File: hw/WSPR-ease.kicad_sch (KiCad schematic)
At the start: 44 parts, among them J101 pwr+data, J102 SMA, J103 SMA, Q101 MMBF170, U101 SRV05-4, U102 ESP32-S3-WROOM-1-N8R8, U103 LMR51430YDDCR, U104 GNSS module

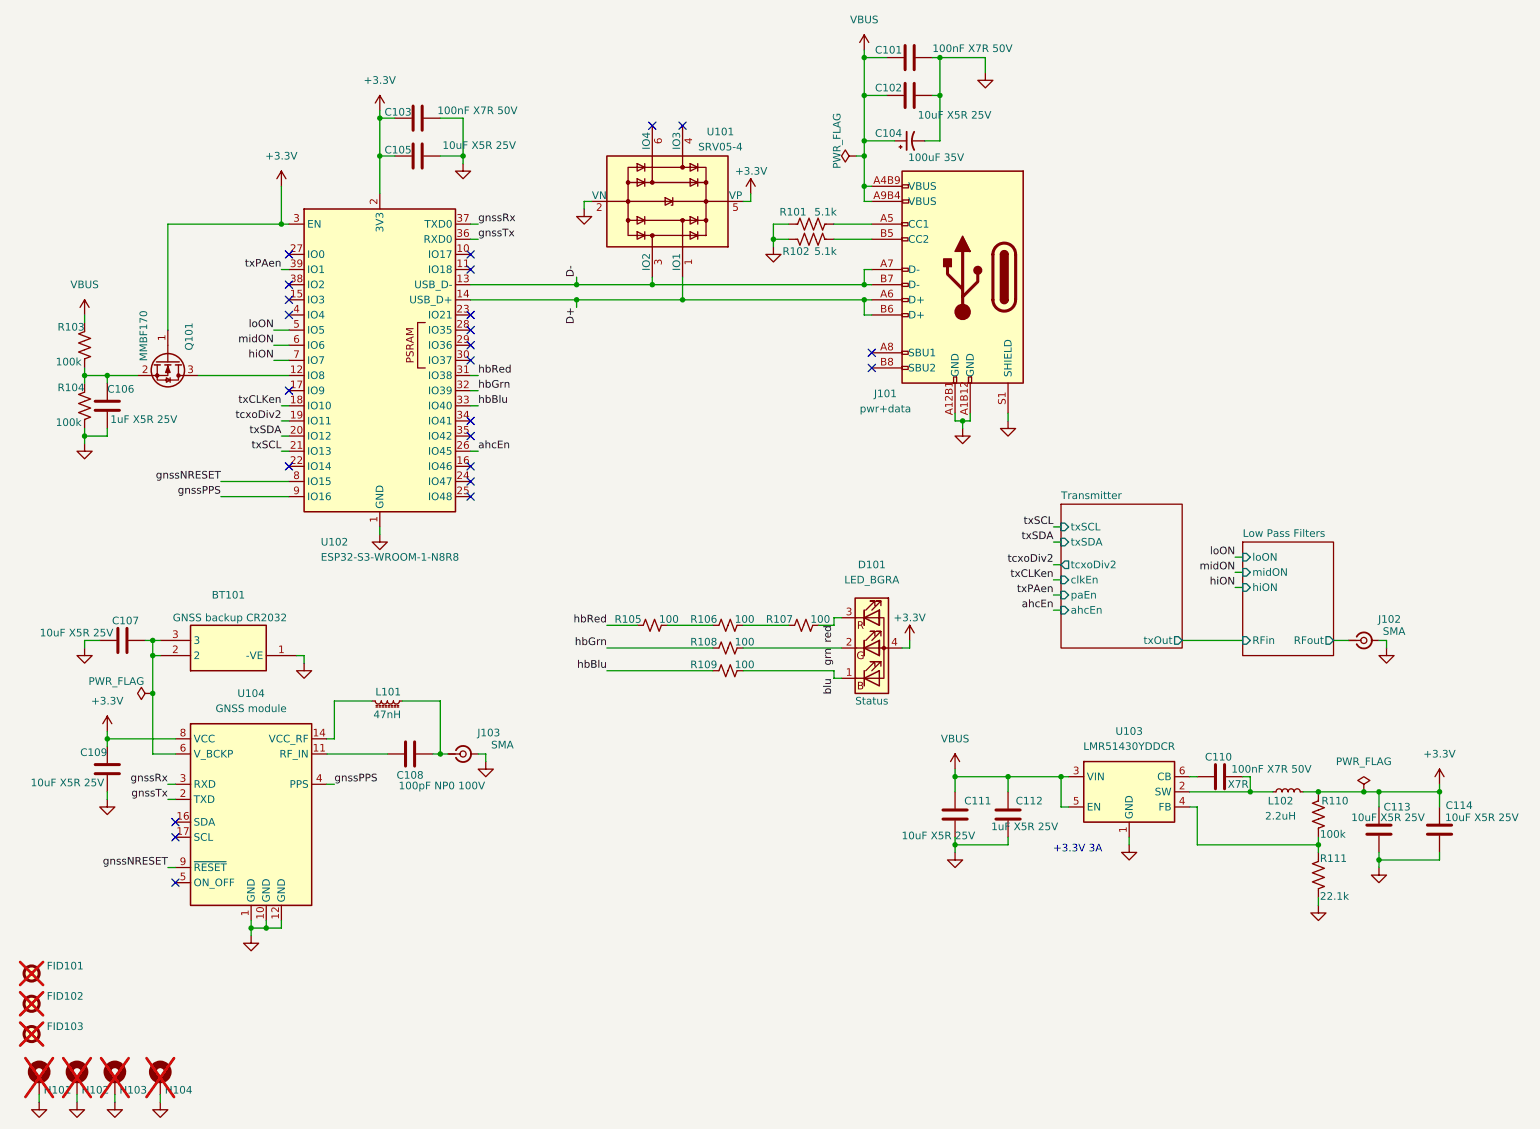
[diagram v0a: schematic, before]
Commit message: Now using RP2040 as a DDS. I can use SPI co-host to program its (SPI) flash. I can use I2C between ESP32 and RP2040 to send commands and receive status.
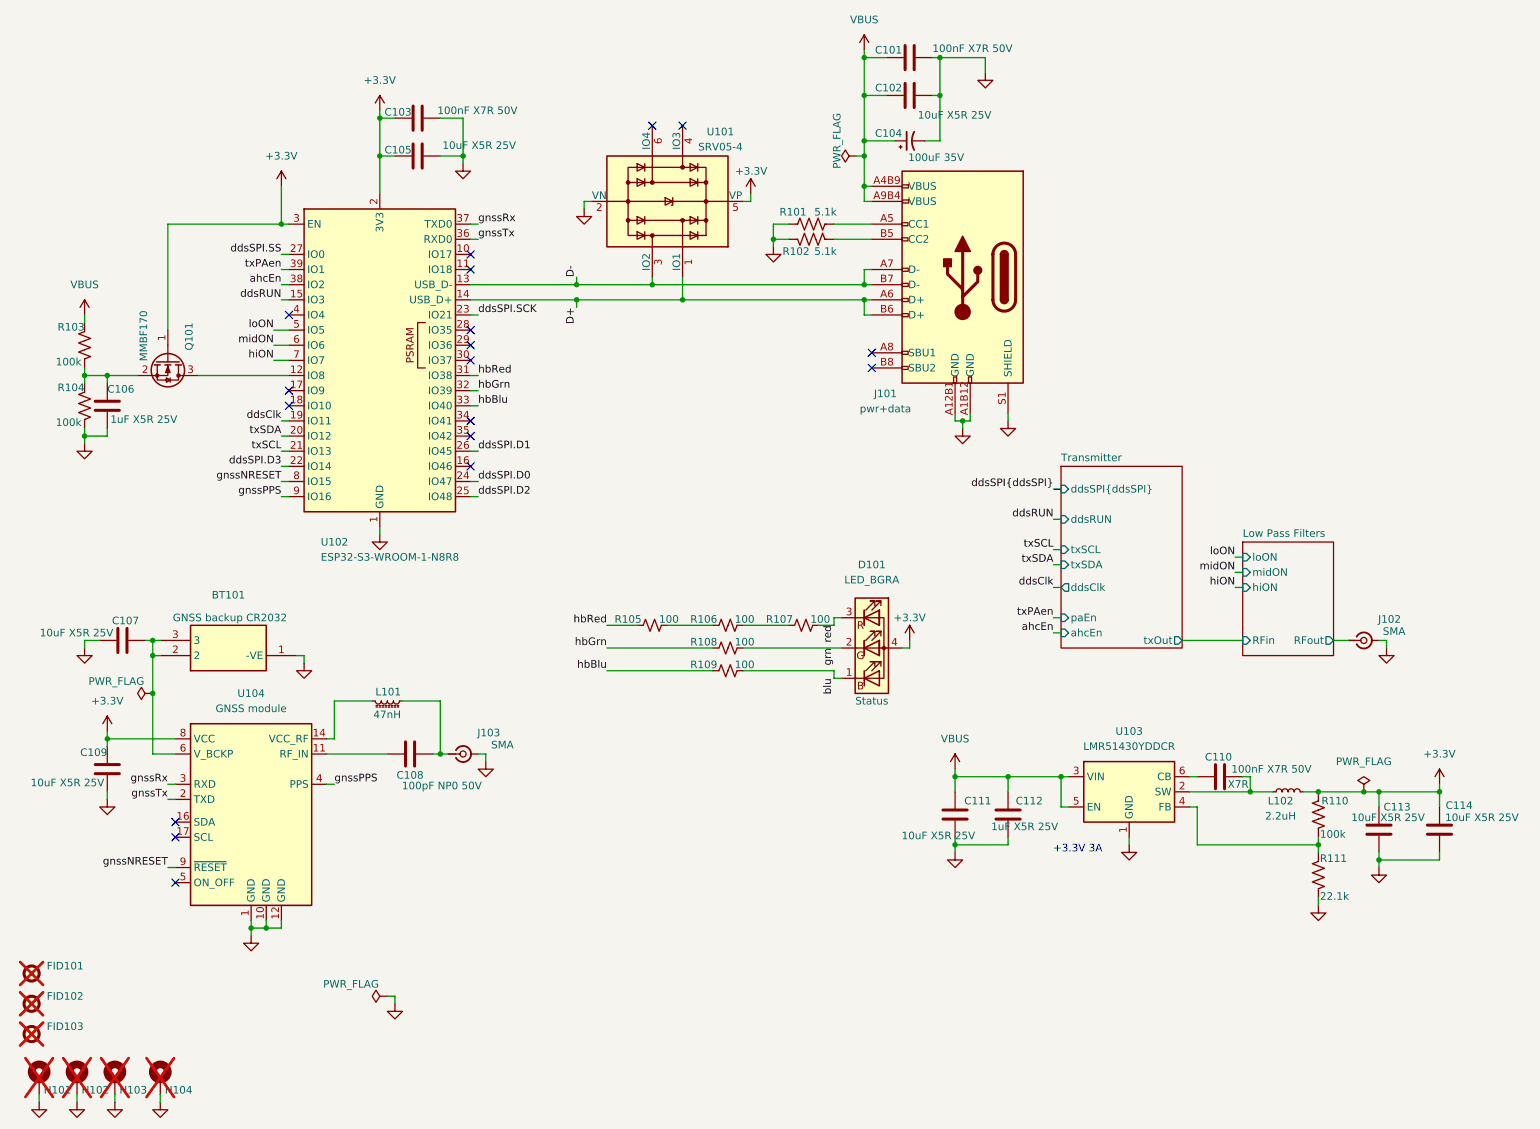
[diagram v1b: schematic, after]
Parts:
- C101, C103, C110: footprint Capacitor_SMD:C_0603_1608Metric -> Capacitor_SMD:C_0402_1005Metric; LCSC C14663 -> (none); MPN KGM15BR71H104KT -> KAM05FR71H104KH; Mouser_PN 581-KGM15BR71H104KT -> (none)
- C108: value 100pF NP0 100V -> 100pF NP0 50V; footprint Capacitor_SMD:C_0603_1608Metric -> Capacitor_SMD:C_0402_1005Metric; LCSC C76709 -> (none); MFG Kyocera AVX -> (none); MPN KGM15ACG2A101FT -> (none); Mouser_PN 581-KGM15ACG2A101FT -> (none)
- R103, R104, R110: LCSC C2906859 -> C2479306; MFG Bourns -> Yageo; MPN CRT0402-FZ-1003GLF -> AC0402FR-0747RL; Mouser_PN 652-CRT0402FZ1003GLF -> 603-AC0402FR-0747RL
- R105, R106, R107, R108, R109: LCSC C2906860 -> (none); MFG Bourns -> Yageo; MPN CR0402-JW-101GLF -> RT0402FRD0722K1L; Mouser_PN 652-CR0402JW-101GLF -> 603-RT0402FRD0722K1L
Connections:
- net ahcEn: now also U102.38 (IO2); no longer U102.26 (IO45)
- net ddsRUN: now reaches U102.15 (IO3)
- net ddsSPI.D3: now reaches U102.22 (IO14)
- net ddsSPI.SCK: now reaches U102.23 (IO21)
- net ddsSPI.D0: now reaches U102.24 (IO47)
- net ddsSPI.D2: now reaches U102.25 (IO48)
- net ddsSPI.SS: now reaches U102.27 (IO0)
- net tcxoDiv2 renamed ddsClk
- net txCLKen: no longer names the net of U102.18 (IO10)
- new net ddsSPI.D1: U102.26 (IO45)
- no-connect marks 24 -> 18
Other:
- sheet Transmitter ports: added ddsClk, ddsRUN, ddsSPI{ddsSPI}; removed clkEn, tcxoDiv2
